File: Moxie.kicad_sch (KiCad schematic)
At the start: 12 parts, among them SW1 SW_Push, SW2 SW_Push, SW3 SW_Push

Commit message: ERC check
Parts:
- added U1: MAX30102, symbol spo2:MAX30102_Module
- added U2: SSD1306, symbol spo2:SSD1306
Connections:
- net +5V: now also U1.5 (VCC), U2.2 (VCC)
- net GND: now also U1.4 (GND), U2.1 (GND)
- net at A1.24 (A5): now also U1.3 (SCL), U2.3 (SCL)
- net at A1.25 (A6): now also U1.2 (SDA), U2.4 (SDA)
- no-connect marks 0 -> 21

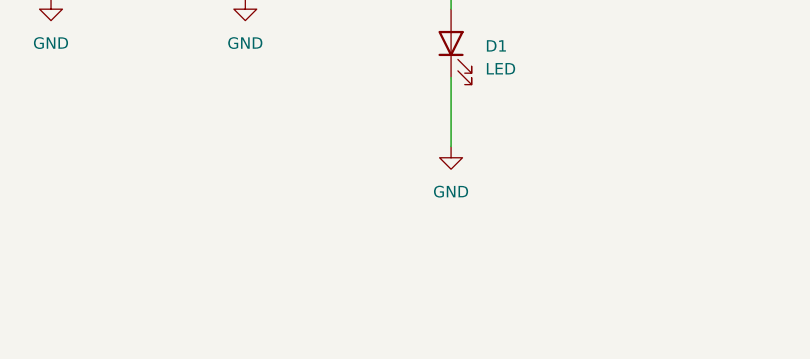
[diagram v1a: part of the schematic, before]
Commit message: custom footprint for MAX30102
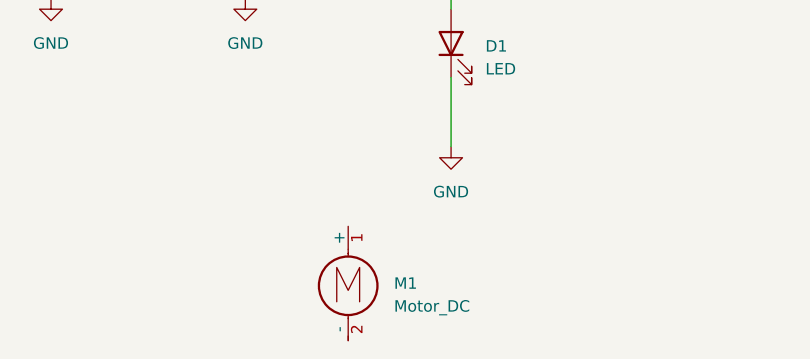
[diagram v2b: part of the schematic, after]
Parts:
- added M1: Motor_DC, symbol Motor:Motor_DC
- C1, C2, C3: footprint (none) -> Capacitor_THT:C_Disc_D7.0mm_W2.5mm_P5.00mm
- D1: footprint (none) -> LED_THT:LED_D5.0mm
- R1, R2, R3, R4: footprint (none) -> Resistor_THT:R_Axial_DIN0207_L6.3mm_D2.5mm_P7.62mm_Horizontal
- SW1, SW2, SW3: footprint (none) -> Button_Switch_THT:SW_PUSH_6mm
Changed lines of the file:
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@@
 			)
 		)
-		(property "Footprint" ""
+		(property "Footprint" "Button_Switch_THT:SW_PUSH_6mm"
 			(at 68.58 106.68 0)
 			(effects
@@
 			)
 		)
-		(property "Footprint" ""
+		(property "Footprint" "Resistor_THT:R_Axial_DIN0207_L6.3mm_D2.5mm_P7.62mm_Horizontal"
 			(at 93.472 83.82 90)
 			(effects
@@
 	)
 	(symbol
+		(lib_id "Motor:Motor_DC")
+		(at 106.68 148.59 0)
+		(unit 1)
+		(exclude_from_sim no)
+		(in_bom yes)
+		(on_board yes)
+		(dnp no)
+		(fields_autoplaced yes)
+		(property "Reference" "M1"
+			(at 111.76 149.8599 0)
+			(effects
+				(font
+					(size 1.27 1.27)
+				)
+				(justify left)
+			)
+		)
+		(property "Value" "Motor_DC"
+			(at 111.76 152.3999 0)
+			(effects
+				(font
+					(size 1.27 1.27)
+				)
+				(justify left)
+			)
+		)
+		(property "Footprint" ""
+			(at 106.68 150.876 0)
+			(effects
+				(font
+					(size 1.27 1.27)
+				)
+				(hide yes)
+			)
+		)
+		(property "Datasheet" "~"
+			(at 106.68 150.876 0)
+			(effects
+				(font
+					(size 1.27 1.27)
+				)
+				(hide yes)
+			)
+		)
+		(property "Description" "DC Motor"
+			(at 106.68 148.59 0)
+			(effects
+				(font
+					(size 1.27 1.27)
+				)
+				(hide yes)
+			)
+		)
+		(pin "1"
+		)
+		(pin "2"
+		)
+		(instances
+			(project ""
+				(path "/7fcaf5d1-8d96-49d6-b380-7df450f94d7a"
+					(reference "M1")
+					(unit 1)
+				)
+			)
+		)
+	)
+	(symbol
 		(lib_id "Device:R")
 		(at 73.66 83.82 0)
@@
 			)
 		)
-		(property "Footprint" ""
+		(property "Footprint" "Resistor_THT:R_Axial_DIN0207_L6.3mm_D2.5mm_P7.62mm_Horizontal"
 			(at 71.882 83.82 90)
 			(effects
@@
 			)
 		)
-		(property "Footprint" ""
+		(property "Footprint" "Capacitor_THT:C_Disc_D7.0mm_W2.5mm_P5.00mm"
 			(at 60.6552 99.06 0)
 			(effects
@@
 			)
 		)
-		(property "Footprint" ""
+		(property "Footprint" "Capacitor_THT:C_Disc_D7.0mm_W2.5mm_P5.00mm"
 			(at 36.5252 100.33 0)
 			(effects
@@
 			)
 		)
-		(property "Footprint" ""
+		(property "Footprint" "LED_THT:LED_D5.0mm"
 			(at 118.11 123.19 0)
 			(effects
@@
 			)
 		)
-		(property "Footprint" ""
+		(property "Footprint" "Capacitor_THT:C_Disc_D7.0mm_W2.5mm_P5.00mm"
 			(at 82.2452 99.06 0)
 			(effects
@@
 			)
 		)
-		(property "Footprint" ""
+		(property "Footprint" "Button_Switch_THT:SW_PUSH_6mm"
 			(at 44.45 107.95 0)
 			(effects
@@
 			)
 		)
-		(property "Footprint" ""
+		(property "Footprint" "Resistor_THT:R_Axial_DIN0207_L6.3mm_D2.5mm_P7.62mm_Horizontal"
 			(at 47.752 85.09 90)
 			(effects
@@
 			)
 		)
-		(property "Footprint" ""
+		(property "Footprint" "Button_Switch_THT:SW_PUSH_6mm"
 			(at 90.17 106.68 0)
 			(effects
@@
 			)
 		)
-		(property "Footprint" ""
+		(property "Footprint" "Resistor_THT:R_Axial_DIN0207_L6.3mm_D2.5mm_P7.62mm_Horizontal"
 			(at 116.332 111.76 90)
 			(effects

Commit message: SSD1306 + assigned footprint
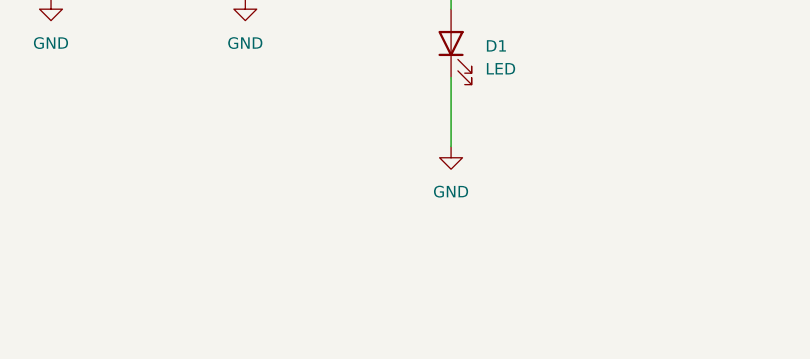
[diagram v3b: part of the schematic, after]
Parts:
- removed M1: Motor_DC, symbol Motor:Motor_DC
- U1: footprint (none) -> spo2:MAX30102_MODULE
- U2: footprint (none) -> spo2:SSD1306
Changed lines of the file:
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@@
 			)
 		)
-		(property "Footprint" ""
+		(property "Footprint" "spo2:MAX30102_MODULE"
 			(at 168.91 120.65 0)
 			(effects
@@
 			)
 		)
-		(property "Footprint" ""
+		(property "Footprint" "spo2:SSD1306"
 			(at 185.42 96.52 0)
 			(effects
@@
 					(unit 1)
 				)
-			)
-		)
-	)
-	(symbol
-		(lib_id "Motor:Motor_DC")
-		(at 106.68 148.59 0)
-		(unit 1)
-		(exclude_from_sim no)
-		(in_bom yes)
-		(on_board yes)
-		(dnp no)
-		(fields_autoplaced yes)
-		(property "Reference" "M1"
-			(at 111.76 149.8599 0)
-			(effects
-				(font
-					(size 1.27 1.27)
-				)
-				(justify left)
-			)
-		)
-		(property "Value" "Motor_DC"
-			(at 111.76 152.3999 0)
-			(effects
-				(font
-					(size 1.27 1.27)
-				)
-				(justify left)
-			)
-		)
-		(property "Footprint" ""
-			(at 106.68 150.876 0)
-			(effects
-				(font
-					(size 1.27 1.27)
-				)
-				(hide yes)
-			)
-		)
-		(property "Datasheet" "~"
-			(at 106.68 150.876 0)
-			(effects
-				(font
-					(size 1.27 1.27)
-				)
-				(hide yes)
-			)
-		)
-		(property "Description" "DC Motor"
-			(at 106.68 148.59 0)
-			(effects
-				(font
-					(size 1.27 1.27)
-				)
-				(hide yes)
-			)
-		)
-		(pin "1"
-		)
-		(pin "2"
-		)
-		(instances
-			(project ""
-				(path "/7fcaf5d1-8d96-49d6-b380-7df450f94d7a"
-					(reference "M1")
-					(unit 1)
-				)
